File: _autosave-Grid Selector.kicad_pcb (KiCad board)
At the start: 2 copper layers, 231.8 x 60.3 mm, 122 parts, among them SW1 MX_SW_HS, SW10 MX_SW_HS, SW11 MX_SW_HS, SW12 MX_SW_HS, SW13 MX_SW_HS, SW14 MX_SW_HS, SW15 MX_SW_HS, SW16 MX_SW_HS, SW17 MX_SW_HS, SW18 MX_SW_HS, SW19 MX_SW_HS, SW2 MX_SW_HS, SW20 MX_SW_HS, SW21 MX_SW_HS, SW22 MX_SW_HS, SW23 MX_SW_HS, SW24 MX_SW_HS, SW25 MX_SW_HS, SW26 MX_SW_HS, SW27 MX_SW_HS, SW28 MX_SW_HS, SW29 MX_SW_HS, SW3 MX_SW_HS, SW30 MX_SW_HS, SW4 MX_SW_HS, SW5 MX_SW_HS, SW6 MX_SW_HS, SW7 MX_SW_HS, SW8 MX_SW_HS, SW9 MX_SW_HS, U1 Pico

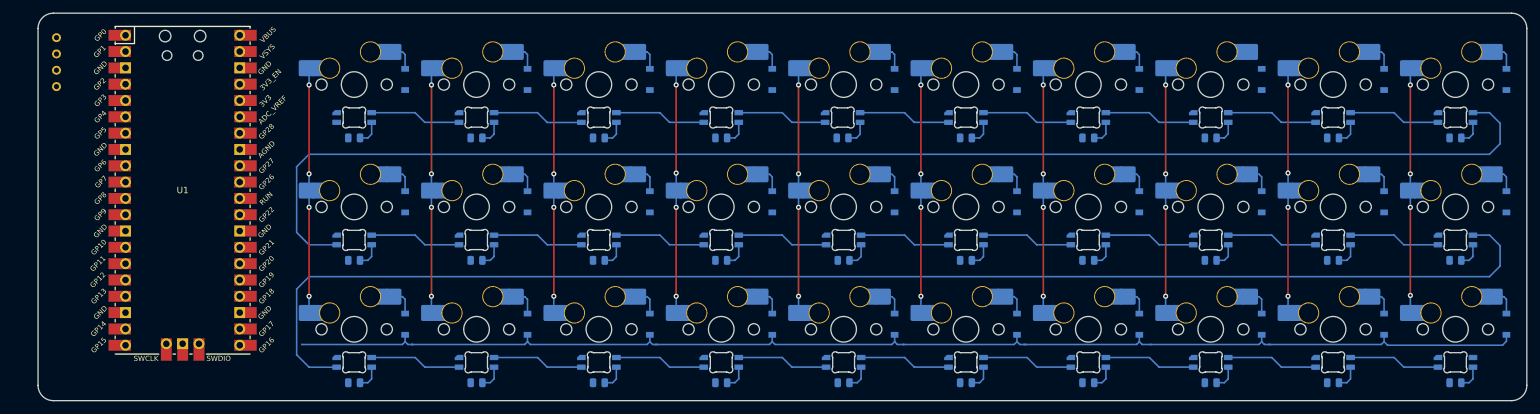
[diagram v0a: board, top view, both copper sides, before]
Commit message: routed switch matrix and led chain
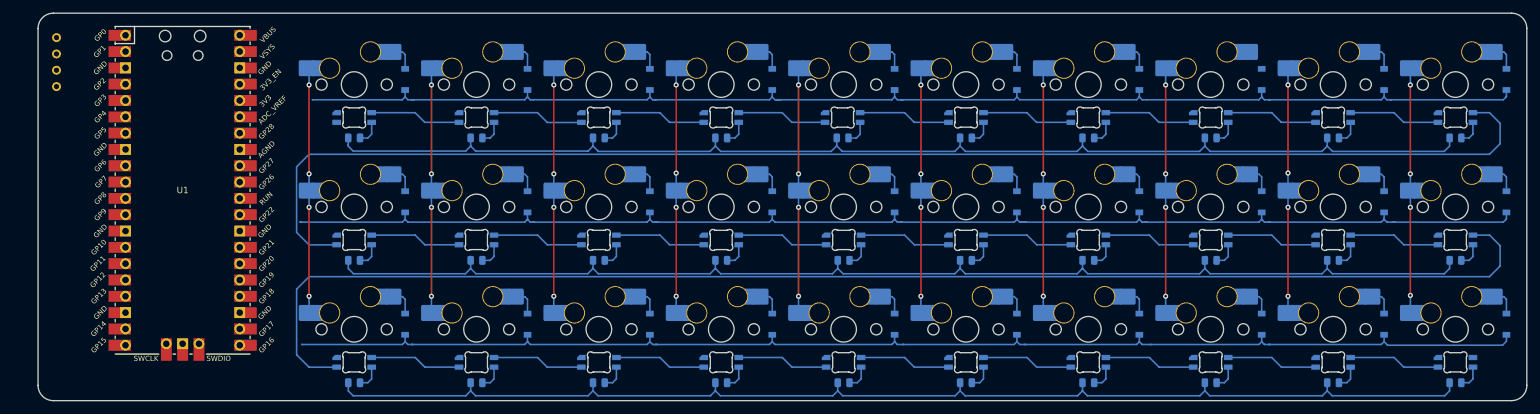
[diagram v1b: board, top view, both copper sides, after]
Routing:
- net +5V: track 0.00 -> 570.4 mm
- net ROW1: track 0.00 -> 204.9 mm
- net ROW0: track 0.00 -> 202.2 mm

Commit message: connected switch matrix and led chain to pico
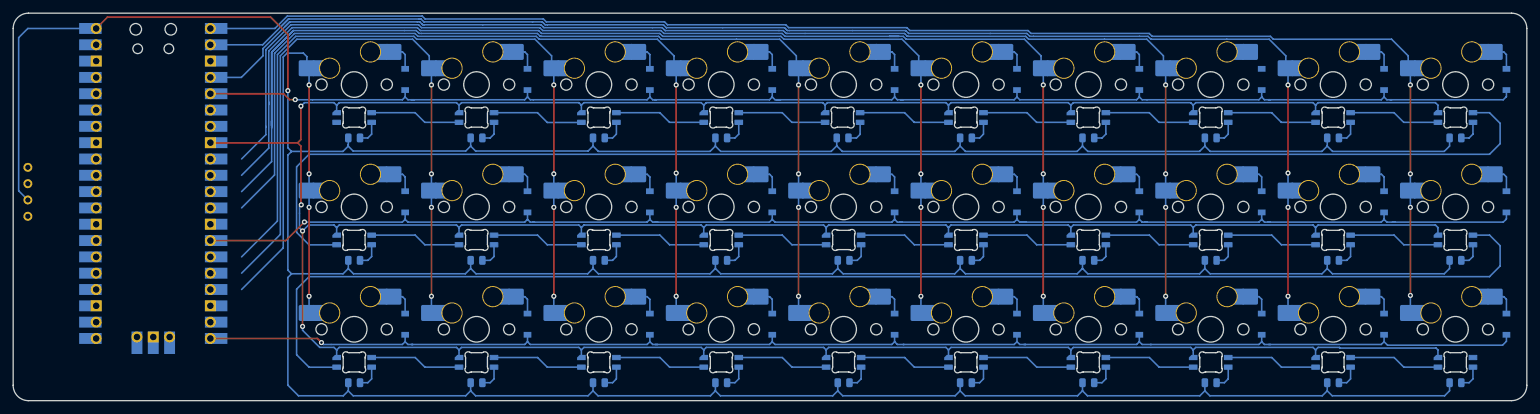
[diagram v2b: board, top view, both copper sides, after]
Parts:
- U1: moved to B.Cu
- moved OL1 20.7 mm to (45.2, 69.1)
- moved U1 4.69 mm to (64.8, 67.8), turned to 180 degrees
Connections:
- SW19 pad 1: Net-(SW19-Pad1) -> COL6
- SW20 pad 1: Net-(SW19-Pad1) -> COL6
- SW21 pad 1: Net-(SW19-Pad1) -> COL6
- SW22 pad 1: Net-(SW22-Pad1) -> COL7
- SW23 pad 1: Net-(SW22-Pad1) -> COL7
- SW24 pad 1: Net-(SW22-Pad1) -> COL7
- SW25 pad 1: Net-(SW25-Pad1) -> COL8
- SW26 pad 1: Net-(SW25-Pad1) -> COL8
- SW27 pad 1: Net-(SW25-Pad1) -> COL8
- SW28 pad 1: Net-(SW28-Pad1) -> COL9
- SW29 pad 1: Net-(SW28-Pad1) -> COL9
- SW30 pad 1: Net-(SW28-Pad1) -> COL9
- U1 pad 1: unconnected-(U1-Pad1) -> COL9
- U1 pad 10: unconnected-(U1-Pad10) -> COL3
- U1 pad 11: unconnected-(U1-Pad11) -> COL2
- U1 pad 12: unconnected-(U1-Pad12) -> COL1
- U1 pad 13: unconnected-(U1-Pad13) -> COL0
- U1 pad 14: unconnected-(U1-Pad14) -> ROW1
- U1 pad 2: unconnected-(U1-Pad2) -> COL8
- U1 pad 20: unconnected-(U1-Pad20) -> ROW2
- U1 pad 31: unconnected-(U1-Pad31) -> SDA
- U1 pad 32: unconnected-(U1-Pad32) -> SCL
- U1 pad 4: unconnected-(U1-Pad4) -> COL7
- U1 pad 5: unconnected-(U1-Pad5) -> ROW0
- U1 pad 6: SDA -> COL6
- U1 pad 7: SCL -> COL5
- U1 pad 8: unconnected-(U1-Pad8) -> GND
- U1 pad 9: unconnected-(U1-Pad9) -> COL4
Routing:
- net GND: track 0.00 -> 626.1 mm, vias 0 -> 4
- net COL9: track 0.00 -> 230.4 mm, vias 0 -> 4
- net COL8: track 0.00 -> 213.6 mm, vias 0 -> 4
- net COL7: track 0.00 -> 196.4 mm, vias 0 -> 4
- net COL6: track 0.00 -> 185.0 mm, vias 0 -> 4
- net +5V: track 570.4 -> 724.8 mm, vias 0 -> 1
- net COL4: track 38.7 -> 169.3 mm
- net COL5: track 38.7 -> 166.6 mm
- net COL3: track 38.7 -> 131.7 mm
- net COL2: track 38.7 -> 119.5 mm
- net COL1: track 38.7 -> 102.3 mm
- net COL0: track 38.7 -> 83.5 mm
- net Net-(SW19-Pad1): track 38.7 -> 0.00 mm, vias 4 -> 0
- net Net-(SW22-Pad1): track 38.7 -> 0.00 mm, vias 4 -> 0
- net Net-(SW25-Pad1): track 38.7 -> 0.00 mm, vias 4 -> 0
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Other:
- board size 231.8 x 60.3 mm -> 235.6 x 60.3 mm
